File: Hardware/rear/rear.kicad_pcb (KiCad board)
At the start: 4 copper layers, 25 x 60 mm, 18 parts, among them J101 Conn_02x10_Odd_Even, J102 USB_B, J103 ARJC07-111071A, U101 AT24CS32-SSHM, U102 WE-TVS-82400102, U103 MCP3021

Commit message: Tweaks to front and rear panel boards
- Minor movement of stuff and silkscreen cleanup for manufacturing
  exporting

- Removed display connector from front panel board; this is now directly
  connected to the controller instead, to make the board a bit simpler
  and reduce the amount of stuff going on
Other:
- board text added: "JLCJLCJLCJLC"
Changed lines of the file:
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@@
       (layerselection 0x00010fc_ffffffff)
       (disableapertmacros false)
-      (usegerberextensions false)
+      (usegerberextensions true)
       (usegerberattributes true)
       (usegerberadvancedattributes true)
@@
       (psa4output false)
       (plotreference true)
-      (plotvalue true)
+      (plotvalue false)
       (plotinvisibletext false)
       (sketchpadsonfab false)
-      (subtractmaskfromsilk false)
+      (subtractmaskfromsilk true)
       (outputformat 1)
       (mirror false)
-      (drillshape 1)
+      (drillshape 0)
       (scaleselection 1)
-      (outputdirectory "")
+      (outputdirectory "/Users/tristan/Electronics/Gerbers/programmable-load/Rev1/rear-io/")
     )
   )
@@
     (fp_line (start -1 -0.625) (end 1 -0.625) (layer "F.Fab") (width 0.1))
     (fp_line (start -1 0.625) (end -1 -0.625) (layer "F.Fab") (width 0.1))
-    (pad "1" smd roundrect (at -1.0375 0) (size 1.175 1.45) (layers "F.Cu" "F.Paste" "F.Mask") (roundrect_rratio 0.212766)
+    (pad "1" smd roundrect (at -1.0375 0) (size 1.175 1.45) (layers "F.Cu" "F.Paste" "F.Mask") (roundrect_rratio 0.2127659574)
       (net 1 "+3V3") (pintype "passive"))
-    (pad "2" smd roundrect (at 1.0375 0) (size 1.175 1.45) (layers "F.Cu" "F.Paste" "F.Mask") (roundrect_rratio 0.212766)
+    (pad "2" smd roundrect (at 1.0375 0) (size 1.175 1.45) (layers "F.Cu" "F.Paste" "F.Mask") (roundrect_rratio 0.2127659574)
       (net 2 "GND") (pintype "passive"))
     (model "${KICAD6_3DMODEL_DIR}/Capacitor_SMD.3dshapes/C_0805_2012Metric.wrl"
@@
     (fp_line (start 1 0.625) (end -1 0.625) (layer "F.Fab") (width 0.1))
     (fp_line (start 1 -0.625) (end 1 0.625) (layer "F.Fab") (width 0.1))
-    (pad "1" smd roundrect (at -1.0375 0 270) (size 1.175 1.45) (layers "F.Cu" "F.Paste" "F.Mask") (roundrect_rratio 0.212766)
+    (pad "1" smd roundrect (at -1.0375 0 270) (size 1.175 1.45) (layers "F.Cu" "F.Paste" "F.Mask") (roundrect_rratio 0.2127659574)
       (net 1 "+3V3") (pintype "passive"))
-    (pad "2" smd roundrect (at 1.0375 0 270) (size 1.175 1.45) (layers "F.Cu" "F.Paste" "F.Mask") (roundrect_rratio 0.212766)
+    (pad "2" smd roundrect (at 1.0375 0 270) (size 1.175 1.45) (layers "F.Cu" "F.Paste" "F.Mask") (roundrect_rratio 0.2127659574)
       (net 2 "GND") (pintype "passive"))
     (model "${KICAD6_3DMODEL_DIR}/Capacitor_SMD.3dshapes/C_0805_2012Metric.wrl"
@@
     (fp_line (start 1 0.625) (end -1 0.625) (layer "F.Fab") (width 0.1))
     (fp_line (start 1 -0.625) (end 1 0.625) (layer "F.Fab") (width 0.1))
-    (pad "1" smd roundrect (at -1 0) (size 1.2 1.4) (layers "F.Cu" "F.Paste" "F.Mask") (roundrect_rratio 0.208333)
+    (pad "1" smd roundrect (at -1 0) (size 1.2 1.4) (layers "F.Cu" "F.Paste" "F.Mask") (roundrect_rratio 0.2083333333)
       (net 27 "Net-(R103-Pad2)") (pintype "passive"))
-    (pad "2" smd roundrect (at 1 0) (size 1.2 1.4) (layers "F.Cu" "F.Paste" "F.Mask") (roundrect_rratio 0.208333)
+    (pad "2" smd roundrect (at 1 0) (size 1.2 1.4) (layers "F.Cu" "F.Paste" "F.Mask") (roundrect_rratio 0.2083333333)
       (net 2 "GND") (pintype "passive"))
     (model "${KICAD6_3DMODEL_DIR}/Resistor_SMD.3dshapes/R_0805_2012Metric.wrl"
@@
     (fp_line (start -1 0.625) (end -1 -0.625) (layer "F.Fab") (width 0.1))
     (fp_line (start 1 0.625) (end -1 0.625) (layer "F.Fab") (width 0.1))
-    (pad "1" smd roundrect (at -1 0 90) (size 1.2 1.4) (layers "F.Cu" "F.Paste" "F.Mask") (roundrect_rratio 0.208333)
+    (pad "1" smd roundrect (at -1 0 90) (size 1.2 1.4) (layers "F.Cu" "F.Paste" "F.Mask") (roundrect_rratio 0.2083333333)
       (net 1 "+3V3") (pintype "passive"))
-    (pad "2" smd roundrect (at 1 0 90) (size 1.2 1.4) (layers "F.Cu" "F.Paste" "F.Mask") (roundrect_rratio 0.208333)
+    (pad "2" smd roundrect (at 1 0 90) (size 1.2 1.4) (layers "F.Cu" "F.Paste" "F.Mask") (roundrect_rratio 0.2083333333)
       (net 21 "Net-(J103-Pad9)") (pintype "passive"))
     (model "${KICAD6_3DMODEL_DIR}/Resistor_SMD.3dshapes/R_0805_2012Metric.wrl"
@@
     (fp_line (start -1 -0.625) (end 1 -0.625) (layer "F.Fab") (width 0.1))
     (fp_line (start 1 -0.625) (end 1 0.625) (layer "F.Fab") (width 0.1))
-    (pad "1" smd roundrect (at -1.0375 0 90) (size 1.175 1.45) (layers "F.Cu" "F.Paste" "F.Mask") (roundrect_rratio 0.212766)
+    (pad "1" smd roundrect (at -1.0375 0 90) (size 1.175 1.45) (layers "F.Cu" "F.Paste" "F.Mask") (roundrect_rratio 0.2127659574)
       (net 1 "+3V3") (pintype "passive"))
-    (pad "2" smd roundrect (at 1.0375 0 90) (size 1.175 1.45) (layers "F.Cu" "F.Paste" "F.Mask") (roundrect_rratio 0.212766)
+    (pad "2" smd roundrect (at 1.0375 0 90) (size 1.175 1.45) (layers "F.Cu" "F.Paste" "F.Mask") (roundrect_rratio 0.2127659574)
       (net 2 "GND") (pintype "passive"))
     (model "${KICAD6_3DMODEL_DIR}/Capacitor_SMD.3dshapes/C_0805_2012Metric.wrl"
@@
     (fp_line (start -1 -0.625) (end 1 -0.625) (layer "F.Fab") (width 0.1))
     (fp_line (start 1 0.625) (end -1 0.625) (layer "F.Fab") (width 0.1))
-    (pad "1" smd roundrect (at -1.0375 0) (size 1.175 1.45) (layers "F.Cu" "F.Paste" "F.Mask") (roundrect_rratio 0.212766)
+    (pad "1" smd roundrect (at -1.0375 0) (size 1.175 1.45) (layers "F.Cu" "F.Paste" "F.Mask") (roundrect_rratio 0.2127659574)
       (net 2 "GND") (pintype "passive"))
-    (pad "2" smd roundrect (at 1.0375 0) (size 1.175 1.45) (layers "F.Cu" "F.Paste" "F.Mask") (roundrect_rratio 0.212766)
+    (pad "2" smd roundrect (at 1.0375 0) (size 1.175 1.45) (layers "F.Cu" "F.Paste" "F.Mask") (roundrect_rratio 0.2127659574)
       (net 24 "Net-(C104-Pad2)") (pintype "passive"))
     (model "${KICAD6_3DMODEL_DIR}/Capacitor_SMD.3dshapes/C_0805_2012Metric.wrl"
@@
     (fp_line (start -1 0.625) (end -1 -0.625) (layer "F.Fab") (width 0.1))
     (fp_line (start 1 -0.625) (end 1 0.625) (layer "F.Fab") (width 0.1))
-    (pad "1" smd roundrect (at -1 0 90) (size 1.2 1.4) (layers "F.Cu" "F.Paste" "F.Mask") (roundrect_rratio 0.208333)
+    (pad "1" smd roundrect (at -1 0 90) (size 1.2 1.4) (layers "F.Cu" "F.Paste" "F.Mask") (roundrect_rratio 0.2083333333)
       (net 1 "+3V3") (pintype "passive"))
-    (pad "2" smd roundrect (at 1 0 90) (size 1.2 1.4) (layers "F.Cu" "F.Paste" "F.Mask") (roundrect_rratio 0.208333)
+    (pad "2" smd roundrect (at 1 0 90) (size 1.2 1.4) (layers "F.Cu" "F.Paste" "F.Mask") (roundrect_rratio 0.2083333333)
       (net 22 "Net-(J103-Pad11)") (pintype "passive"))
     (model "${KICAD6_3DMODEL_DIR}/Resistor_SMD.3dshapes/R_0805_2012Metric.wrl"
@@
     (fp_line (start -1 0.625) (end -1 -0.625) (layer "F.Fab") (width 0.1))
     (fp_line (start 1 -0.625) (end 1 0.625) (layer "F.Fab") (width 0.1))
-    (pad "1" smd roundrect (at -1 0) (size 1.2 1.4) (layers "F.Cu" "F.Paste" "F.Mask") (roundrect_rratio 0.208333)
+    (pad "1" smd roundrect (at -1 0) (size 1.2 1.4) (layers "F.Cu" "F.Paste" "F.Mask") (roundrect_rratio 0.2083333333)
       (net 15 "VBUS") (pintype "passive"))
-    (pad "2" smd roundrect (at 1 0) (size 1.2 1.4) (layers "F.Cu" "F.Paste" "F.Mask") (roundrect_rratio 0.208333)
+    (pad "2" smd roundrect (at 1 0) (size 1.2 1.4) (layers "F.Cu" "F.Paste" "F.Mask") (roundrect_rratio 0.2083333333)
       (net 27 "Net-(R103-Pad2)") (pintype "passive"))
     (model "${KICAD6_3DMODEL_DIR}/Resistor_SMD.3dshapes/R_0805_2012Metric.wrl"
@@
     (fp_line (start 1 -0.625) (end 1 0.625) (layer "F.Fab") (width 0.1))
     (fp_line (start 1 0.625) (end -1 0.625) (layer "F.Fab") (width 0.1))
-    (pad "1" smd roundrect (at -1.0375 0 270) (size 1.175 1.45) (layers "F.Cu" "F.Paste" "F.Mask") (roundrect_rratio 0.212766)
+    (pad "1" smd roundrect (at -1.0375 0 270) (size 1.175 1.45) (layers "F.Cu" "F.Paste" "F.Mask") (roundrect_rratio 0.2127659574)
       (net 2 "GND") (pintype "passive"))
-    (pad "2" smd roundrect (at 1.0375 0 270) (size 1.175 1.45) (layers "F.Cu" "F.Paste" "F.Mask") (roundrect_rratio 0.212766)
+    (pad "2" smd roundrect (at 1.0375 0 270) (size 1.175 1.45) (layers "F.Cu" "F.Paste" "F.Mask") (roundrect_rratio 0.2127659574)
       (net 23 "Net-(C103-Pad2)") (pintype "passive"))
     (model "${KICAD6_3DMODEL_DIR}/Capacitor_SMD.3dshapes/C_0805_2012Metric.wrl"
@@
   (gr_line (start 52.5 25) (end 52.5 85) (layer "Edge.Cuts") (width 0.1))
   (gr_line (start 27.5 85) (end 27.5 25) (layer "Edge.Cuts") (width 0.1))
+  (gr_text "JLCJLCJLCJLC" (at 40.05 71) (layer "B.SilkS")
+    (effects (font (size 1 1) (thickness 0.15)) (justify mirror))
+  )
   (gr_text "Programmable Load\nRear I/O" (at 40 34.75) (layer "F.SilkS")
     (effects (font (size 1.5 1.5) (thickness 0.25) italic))

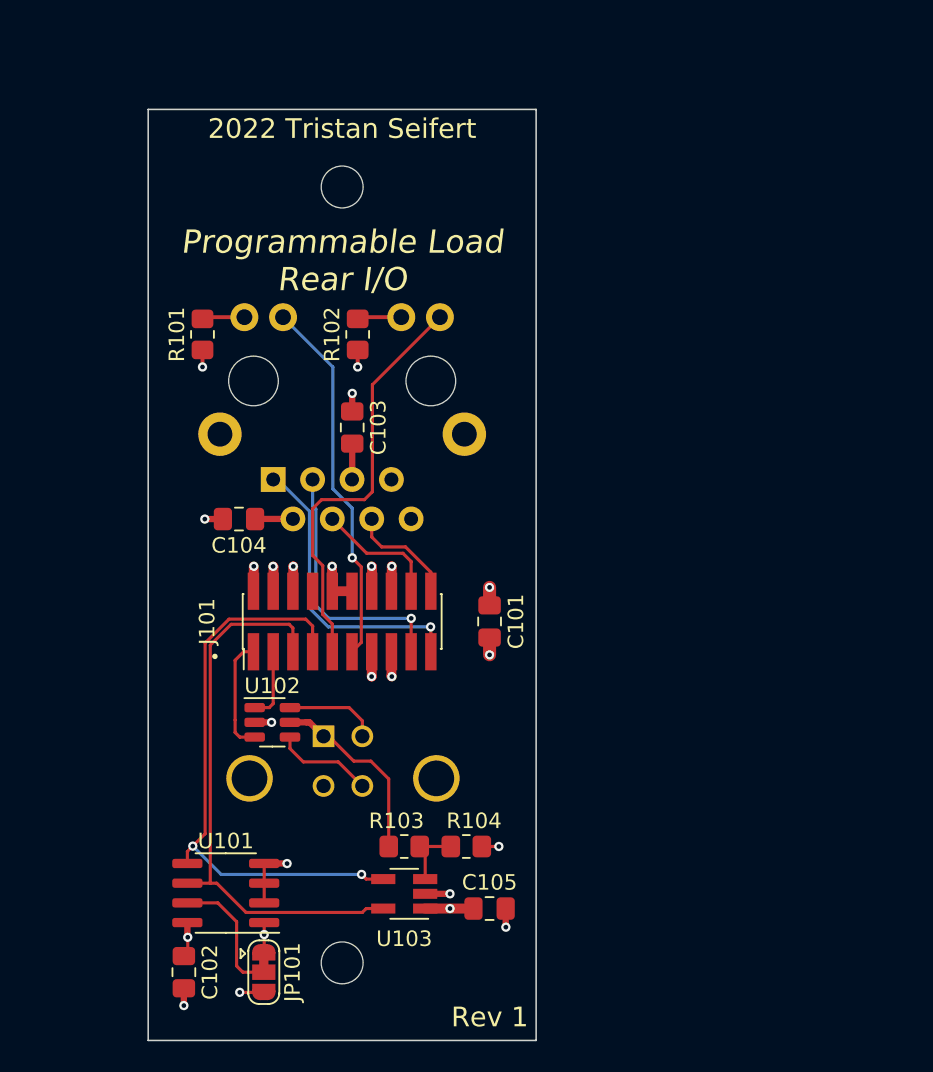
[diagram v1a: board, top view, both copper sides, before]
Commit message: More new layout stuff
- More work on the new controller board layout

- Rework rear IO board for the new Technomet rear panel (it has an
  expansion connector for CAN also, and features four screw holes
  instead of two)

- Added a few footprints (expansion RJ45 connector; some
  horizontal/vertical headers)
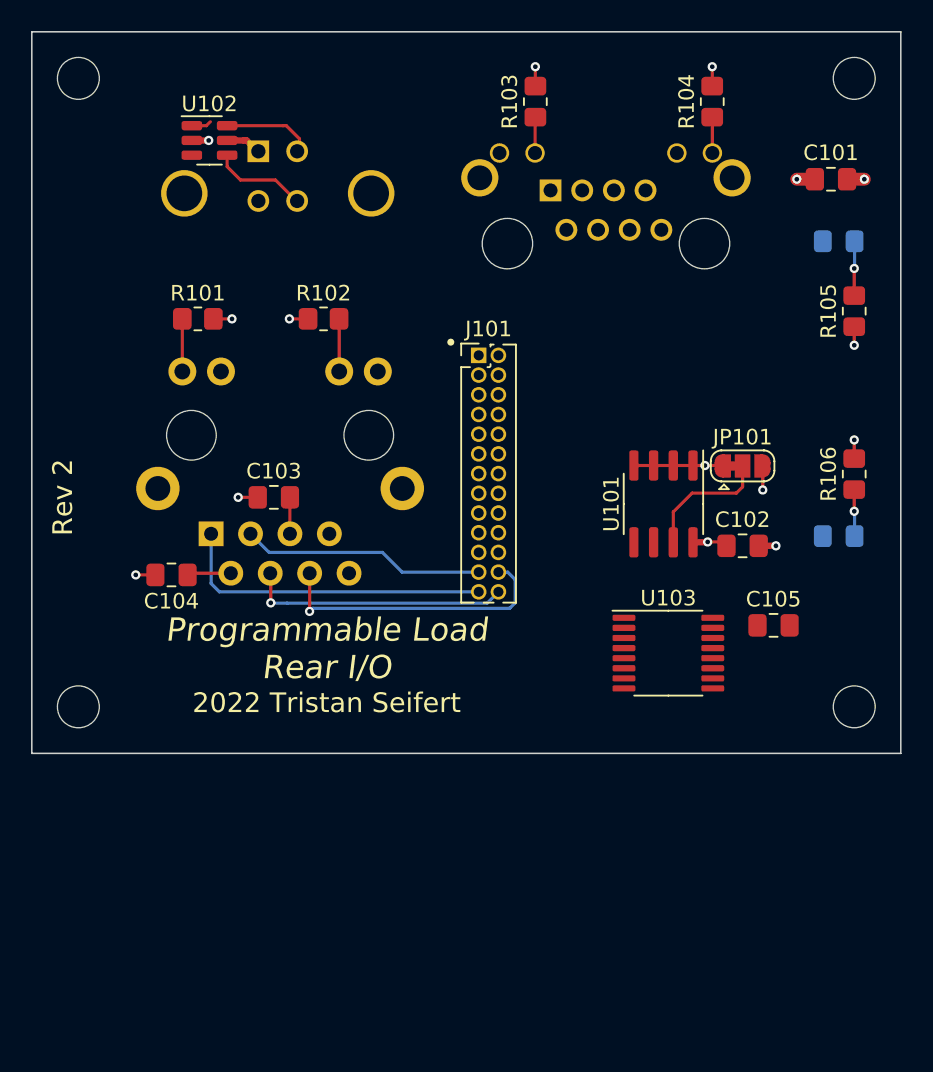
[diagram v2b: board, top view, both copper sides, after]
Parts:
- added D101: Green, LED_SMD:LED_0805_2012Metric_Pad1.15x1.40mm_HandSolder, B.Cu at (72.0, 33.5)
- added D102: Green, LED_SMD:LED_0805_2012Metric_Pad1.15x1.40mm_HandSolder, B.Cu at (72.0, 52.5)
- added H103: MountingHole, MountingHole:MountingHole_2.7mm_M2.5, F.Cu at (73.0, 63.5)
- added H104: MountingHole, MountingHole:MountingHole_2.7mm_M2.5, F.Cu at (23.0, 63.5)
- added J104: CRJ061-L1-TH, programmable-load:CUI_CRJ061-L1-TH, B.Cu at (57.0, 33.6)
- added R105: 1k, Resistor_SMD:R_0805_2012Metric_Pad1.20x1.40mm_HandSolder, F.Cu at (73.0, 38.0)
- added R106: 1k, Resistor_SMD:R_0805_2012Metric_Pad1.20x1.40mm_HandSolder, F.Cu at (73.0, 48.5)
- J101: footprint Connector_PinHeader_1.27mm:PinHeader_2x10_P1.27mm_Vertical_SMD -> Connector_PinHeader_1.27mm:PinHeader_2x13_P1.27mm_Vertical
- R103: value 7k5 -> 100R
- R104: value 12k -> 100R
- U103: value MCP3021 -> XRA1200; footprint Package_TO_SOT_SMD:SOT-23-5_HandSoldering -> Package_SO:TSSOP-16_4.4x5mm_P0.65mm
- moved H102 65.9 mm to (73.0, 23.0)
- moved R104 50.5 mm to (63.9, 24.5), turned to 90 degrees
- moved R103 48.7 mm to (52.5, 24.5), turned to 90 degrees
- moved C102 45.3 mm to (65.8, 53.1), turned to 0 degrees
- moved JP101 44.9 mm to (65.8, 48.0), turned to 0 degrees
- moved J102 37.9 mm to (34.6, 27.7)
- moved U101 37.7 mm to (60.7, 50.4), turned to -90 degrees
- moved U102 37.7 mm to (31.4, 27.0)
- moved C101 36.0 mm to (71.5, 29.5), turned to 180 degrees
- moved C105 25.8 mm to (67.8, 58.2)
- moved U103 23.0 mm to (61.0, 60.0), turned to 0 degrees
- moved J101 19.3 mm to (48.8, 40.9), turned to 0 degrees
- moved H101 18.4 mm to (23.0, 23.0)
- moved C103 6.76 mm to (35.6, 50.0), turned to 0 degrees
- moved C104 5.65 mm to (29.0, 55.0)
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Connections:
- J101 pad 17: /ETH_TX- -> unconnected-(J101-Pad17)
- J101 pad 18: /ETH_RX+ -> /CAN-
- J101 pad 19: /ETH_TX+ -> unconnected-(J101-Pad19)
- J101 pad 20: /ETH_RX- -> /CAN+
- J101 pad 5: /SCL -> /SDA
- J101 pad 7: /SDA -> /~{IRQ}
- J101 pad 8: /~{IRQ} -> /SCL
- R103 pad 1: VBUS -> Net-(J104-Pad10)
- R103 pad 2: Net-(R103-Pad2) -> +3V3
- R104 pad 1: Net-(R103-Pad2) -> Net-(J104-Pad12)
- R104 pad 2: GND -> +3V3
- U103 pad 1: +3V3 -> GND
- U103 pad 3: Net-(R103-Pad2) -> GND
- U103 pad 4: /SDA -> unconnected-(U103-Pad4)
- U103 pad 5: /SCL -> unconnected-(U103-Pad5)
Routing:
- net /SDA: track 37.2 -> 0.00 mm, vias 2 -> 0
- net /SCL: track 36.4 -> 0.00 mm
- net /ETH_LED1: track 27.1 -> 0.00 mm
- net /ETH_LED0: track 23.9 -> 0.00 mm, vias 1 -> 0
- net GND: track 27.4 -> 12.3 mm, vias 17 -> 6
- net /ETH_RX-: track 7.14 -> 18.7 mm, vias 0 -> 1
- net VBUS: track 12.2 -> 2.54 mm
- net /ETH_RX+: track 8.13 -> 16.9 mm, vias 0 -> 1
- net /USB_D+: track 7.45 -> 0.00 mm
- net Net-(R103-Pad2): track 4.24 -> 0.00 mm
- net /USB_D-: track 5.14 -> 1.30 mm
- net Net-(D101-Pad2): track 0.00 -> 3.51 mm, vias 0 -> 1
- net Net-(D102-Pad2): track 0.00 -> 3.01 mm, vias 0 -> 1
- net Net-(J104-Pad10): track 0.00 -> 2.32 mm
- net Net-(J104-Pad12): track 0.00 -> 2.31 mm
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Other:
- board size 25 x 60 mm -> 56 x 46.5 mm
- board text added: "Rev 2"
- board text removed: "Rev 1"
